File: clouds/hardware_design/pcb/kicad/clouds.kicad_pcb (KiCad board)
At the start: 2 copper layers, 88.9 x 106 mm, 156 parts, among them IC1 74HC595D, IC10 TL072D, IC2 LM1117-3.3, IC3 MCP6002, IC4 MCP6004, IC5 STM32F405RGT6, IC6 LM4040B10, IC7 LM1117-3.3, IC8 WM8731, IC9 TL072D, J1 PJ301_THONKICONN6, J10 PJ301_THONKICONN6, J11 PJ301_THONKICONN6, J12 PJ301_THONKICONN6, J2 PJ301_THONKICONN6, J3 PJ301_THONKICONN6, J4 PJ301_THONKICONN6, J5 PJ301_THONKICONN6, J6 PJ301_THONKICONN6, J7 PJ301_THONKICONN6, J8 PJ301_THONKICONN6, J9 PJ301_THONKICONN6, Q1 MMBT3904, Q2 MMBT3904, Q3 8MHz, Q4 12.288MHz, SW1 LP4OA1PBCT

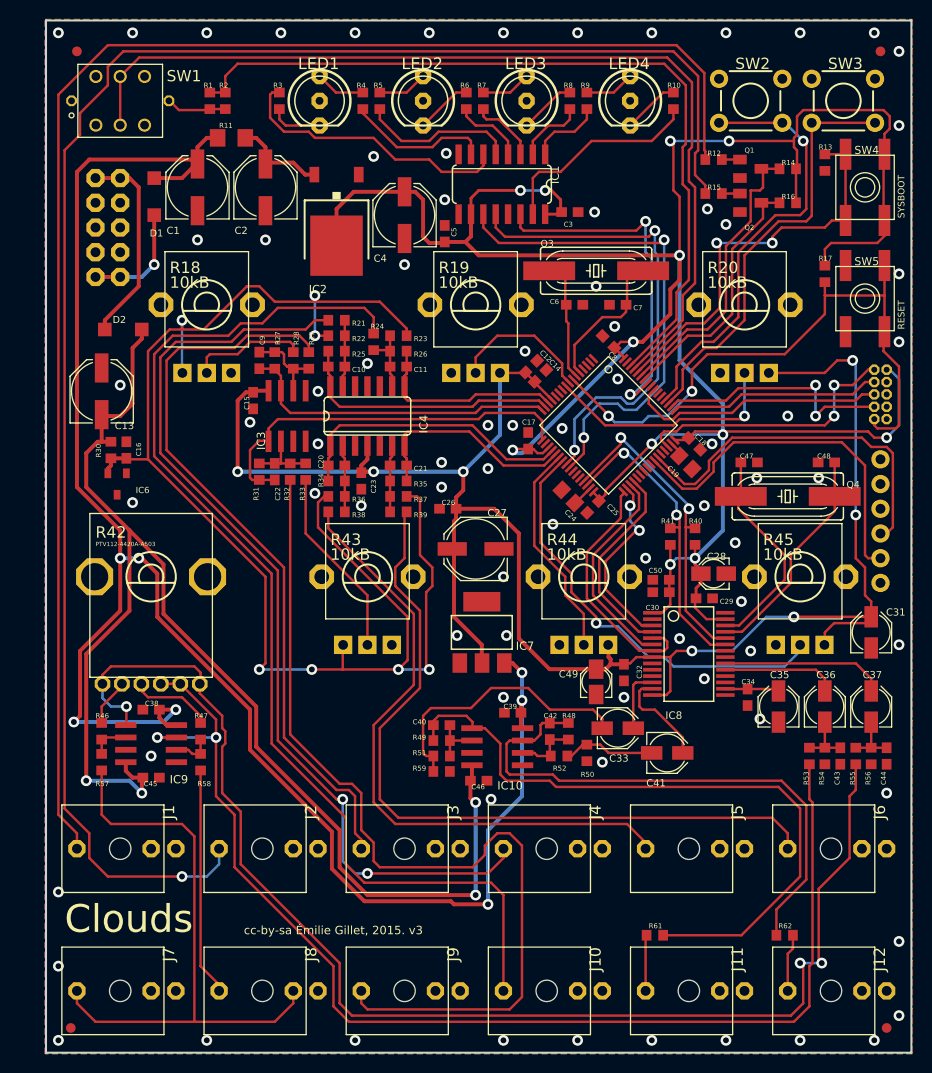
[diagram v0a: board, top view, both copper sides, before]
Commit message: clouds wm8731 QFN on PCB. also panasonic a -> b caps
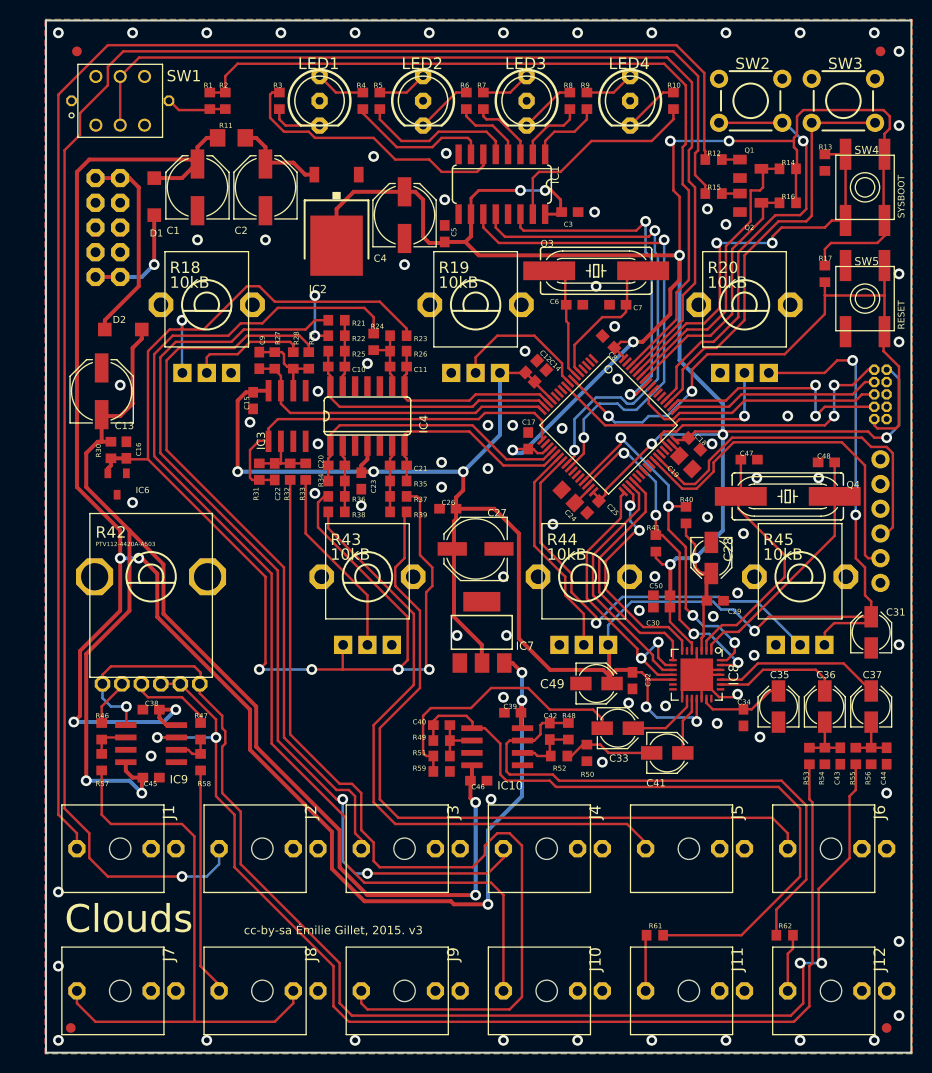
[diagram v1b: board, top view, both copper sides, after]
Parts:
- removed U$2: , clouds:ROHS_BIG
- C28, C49: footprint clouds:PANASONIC_A -> clouds:PANASONIC_B
- IC1: value 74HC595D -> 74595D
- IC8: footprint clouds:SSOP28 -> Package_DFN_QFN:QFN-28-1EP_5x5mm_P0.5mm_EP3.35x3.35mm
- JP1: value (none) -> M06SIP
- SW2, SW3: value (none) -> TAC_SWITCHPTH
- SW4, SW5: value (none) -> EVQQ2
- moved R40 2.39 mm to (169.8, 102.8)
- moved C34 2.13 mm to (175.7, 123.6)
- moved IC8 1.99 mm to (170.9, 119.2)
- moved R41 1.64 mm to (166.7, 105.7)
- moved C28 1.63 mm to (172.4, 107.2), turned to -90 degrees
- moved C30 1.58 mm to (167.3, 112.3)
- moved C50 1.58 mm to (167.3, 111.0)
- moved C32 1.20 mm to (164.3, 119.8)
- moved C29 1.15 mm to (172.8, 111.6)
- moved C47 0.28 mm to (176.3, 97.1)
- moved C49 0.18 mm to (160.6, 120.1), turned to 0 degrees
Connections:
- net BOOT_FLASH renamed /clouds_2/BOOT_FLASH
- net JTCK renamed /clouds_2/JTCK
- net JTDI renamed /clouds_2/JTDI
- net JTDO renamed /clouds_2/JTDO
- net JTMS renamed /clouds_2/JTMS
- net LOUT_JACK renamed Net-(J11-PadP3)
- net RESET renamed /clouds_2/RESET
- net ROUT_JACK renamed Net-(J12-PadP3)
- net RX renamed /clouds_2/RX
- net TX renamed /clouds_2/TX
- C34 pad 1: N$17 -> Net-(C34-Pad1)
- C35 pad +: N$17 -> Net-(C34-Pad1)
- C47 pad 2: N$59 -> Net-(C47-Pad2)
- C48 pad 2: N$60 -> Net-(C48-Pad2)
- IC1 pad 9: (no net) -> unconnected-(IC1-Pad9)
- IC5 pad 10: (no net) -> unconnected-(IC5-Pad10)
- IC5 pad 11: (no net) -> unconnected-(IC5-Pad11)
- IC5 pad 2: (no net) -> unconnected-(IC5-Pad2)
- IC5 pad 27: (no net) -> unconnected-(IC5-Pad27)
- IC5 pad 29: I2C_SCL -> /clouds_2/I2C_SCL
- IC5 pad 3: (no net) -> unconnected-(IC5-Pad3)
- IC5 pad 30: I2C_SDA -> /clouds_2/I2C_SDA
- IC5 pad 33: I2S_LRCK -> /clouds_2/I2S_LRCK
- IC5 pad 34: I2S_SCK -> /clouds_2/I2S_SCK
- IC5 pad 35: I2S_SIN -> /clouds_2/I2S_SIN
- IC5 pad 36: I2S_SOUT -> /clouds_2/I2S_SOUT
- IC5 pad 37: (no net) -> unconnected-(IC5-Pad37)
- IC5 pad 38: (no net) -> unconnected-(IC5-Pad38)
- IC5 pad 39: (no net) -> unconnected-(IC5-Pad39)
- IC5 pad 4: (no net) -> unconnected-(IC5-Pad4)
- IC5 pad 40: (no net) -> unconnected-(IC5-Pad40)
- IC5 pad 41: (no net) -> unconnected-(IC5-Pad41)
- IC5 pad 44: (no net) -> unconnected-(IC5-Pad44)
- IC5 pad 45: (no net) -> unconnected-(IC5-Pad45)
- IC5 pad 53: (no net) -> unconnected-(IC5-Pad53)
- IC5 pad 54: (no net) -> unconnected-(IC5-Pad54)
- IC5 pad 56: (no net) -> unconnected-(IC5-Pad56)
- IC8 pad 1: +3V3 -> Net-(C48-Pad2)
- IC8 pad 10: (no net) -> /clouds_2/I2S_SIN
- IC8 pad 11: GND -> /clouds_2/I2S_LRCK
- IC8 pad 12: LOUT -> +3V3_A
- IC8 pad 13: ROUT -> unconnected-(IC8-Pad13)
- IC8 pad 14: +3V3_A -> unconnected-(IC8-Pad14)
- IC8 pad 16: N$17 -> LOUT
- IC8 pad 17: (no net) -> ROUT
- IC8 pad 18: (no net) -> +3V3_A
- IC8 pad 19: RIN -> GND
- IC8 pad 2: (no net) -> Net-(C47-Pad2)
- IC8 pad 20: LIN -> Net-(C34-Pad1)
- IC8 pad 21: GND -> unconnected-(IC8-Pad21)
- IC8 pad 22: GND -> unconnected-(IC8-Pad22)
- IC8 pad 23: I2C_SDA -> RIN
- IC8 pad 24: I2C_SCL -> LIN
- IC8 pad 25: N$60 -> GND
- IC8 pad 26: N$59 -> GND
- IC8 pad 27: +3V3 -> /clouds_2/I2C_SDA
- IC8 pad 28: GND -> /clouds_2/I2C_SCL
- IC8 pad 3: I2S_SCK -> +3V3
- IC8 pad 4: I2S_SOUT -> GND
- IC8 pad 5: I2S_LRCK -> +3V3
- IC8 pad 6: I2S_SIN -> unconnected-(IC8-Pad6)
- IC8 pad 7: I2S_LRCK -> /clouds_2/I2S_SCK
- IC8 pad 8: +3V3_A -> /clouds_2/I2S_SOUT
- IC8 pad 9: (no net) -> /clouds_2/I2S_LRCK
- J10 pad P2: (no net) -> unconnected-(J10-PadP2)
- J11 pad P2: (no net) -> unconnected-(J11-PadP2)
- J12 pad P2: (no net) -> unconnected-(J12-PadP2)
- J3 pad P2: (no net) -> unconnected-(J3-PadP2)
- J4 pad P2: (no net) -> unconnected-(J4-PadP2)
- J5 pad P2: (no net) -> unconnected-(J5-PadP2)
- J6 pad P2: (no net) -> unconnected-(J6-PadP2)
- J7 pad P2: (no net) -> unconnected-(J7-PadP2)
- J9 pad P2: (no net) -> unconnected-(J9-PadP2)
- JP1 pad 2: (no net) -> unconnected-(JP1-Pad2)
- JP1 pad 3: (no net) -> unconnected-(JP1-Pad3)
- JP1 pad 6: (no net) -> unconnected-(JP1-Pad6)
- JP2 pad 7: (no net) -> unconnected-(JP2-Pad7)
- Q4 pad 1: N$59 -> Net-(C47-Pad2)
- Q4 pad 2: N$60 -> Net-(C48-Pad2)
- R40 pad 1: I2C_SCL -> /clouds_2/I2C_SCL
- R41 pad 1: I2C_SDA -> /clouds_2/I2C_SDA
- SW1 pad P1: (no net) -> unconnected-(SW1-PadP1)
- SW1 pad P4: (no net) -> unconnected-(SW1-PadP4)
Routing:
- net /clouds_2/I2C_SCL: track 0.00 -> 37.5 mm, vias 0 -> 4
- net /clouds_2/I2C_SDA: track 0.00 -> 35.0 mm, vias 0 -> 4
- net I2C_SCL: track 33.2 -> 0.00 mm, vias 2 -> 0
- net I2C_SDA: track 31.3 -> 0.00 mm, vias 2 -> 0
- net /clouds_2/I2S_LRCK: track 0.00 -> 30.8 mm, vias 0 -> 2
- net I2S_LRCK: track 25.5 -> 0.00 mm
- net /clouds_2/I2S_SOUT: track 0.00 -> 25.5 mm
- net /clouds_2/I2S_SIN: track 0.00 -> 25.4 mm
- net Net-(C48-Pad2): track 0.00 -> 25.2 mm
- net Net-(C47-Pad2): track 0.00 -> 25.0 mm
- net /clouds_2/I2S_SCK: track 0.00 -> 23.9 mm, vias 0 -> 2
- net N$60: track 23.2 -> 0.00 mm
- net N$59: track 22.3 -> 0.00 mm
- net I2S_SIN: track 21.9 -> 0.00 mm
- net I2S_SOUT: track 21.1 -> 0.00 mm
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
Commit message: cap spacing
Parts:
- moved C32 0.20 mm to (164.5, 119.8)
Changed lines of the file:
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@@
   )
   (footprint "clouds:C0603" (layer "F.Cu")
-    (at 164.3 119.8 -90)
+    (at 164.5 119.8 -90)
     (descr "<b>CAPACITOR</b>")
     (property "Sheetfile" "clouds_2.kicad_sch")
@@
   (segment (start 143.8411 129.1336) (end 143.8411 127.5461) (width 0.254) (layer "F.Cu") (net 14))
   (segment (start 152.6286 104.6861) (end 152.6286 115.4811) (width 0.4064) (layer "F.Cu") (net 15))
-  (segment (start 162.6 118.7) (end 164.05 118.7) (width 0.4064) (layer "F.Cu") (net 15))
   (segment (start 161.9 120.1) (end 161.9 119.4) (width 0.4064) (layer "F.Cu") (net 15))
   (segment (start 137.0711 97.0661) (end 137.0711 95.6945) (width 0.4064) (layer "F.Cu") (net 15))
@@
   (segment (start 186.9186 86.9061) (end 185.3311 86.9061) (width 0.254) (layer "F.Cu") (net 15))
   (segment (start 188.8236 111.6711) (end 188.1886 111.0361) (width 0.254) (layer "F.Cu") (net 15))
-  (segment (start 164.05 118.7) (end 164.3 118.95) (width 0.4064) (layer "F.Cu") (net 15))
   (segment (start 145.9611 103.4161) (end 145.9611 106.0961) (width 0.4064) (layer "F.Cu") (net 15))
   (segment (start 188.1886 108.1786) (end 187.2361 107.2261) (width 0.254) (layer "F.Cu") (net 15))
+  (segment (start 162.35 118.95) (end 164.3 118.95) (width 0.4064) (layer "F.Cu") (net 15))
   (segment (start 150.0886 102.1461) (end 152.6286 104.6861) (width 0.4064) (layer "F.Cu") (net 15))
   (segment (start 161.9 116.235) (end 161.7961 116.1311) (width 0.4064) (layer "F.Cu") (net 15))
@@
   (segment (start 145.9611 113.2586) (end 148.8186 116.1161) (width 0.4064) (layer "F.Cu") (net 15))
   (segment (start 187.2361 107.2261) (end 187.2361 102.7811) (width 0.254) (layer "F.Cu") (net 15))
+  (segment (start 161.9 119.4) (end 162.35 118.95) (width 0.4064) (layer "F.Cu") (net 15))
   (segment (start 185.3311 86.9061) (end 184.0461 88.1911) (width 0.254) (layer "F.Cu") (net 15))
   (segment (start 123.7361 98.3361) (end 123.7361 91.0336) (width 0.4064) (layer "F.Cu") (net 15))
@@
   (segment (start 188.1886 111.0361) (end 188.1886 108.1786) (width 0.254) (layer "F.Cu") (net 15))
   (segment (start 146.9136 98.3361) (end 146.9136 100.2411) (width 0.4064) (layer "F.Cu") (net 15))
-  (segment (start 161.9 119.4) (end 162.6 118.7) (width 0.4064) (layer "F.Cu") (net 15))
   (segment (start 136.4361 97.7011) (end 137.0711 97.0661) (width 0.4064) (layer "F.Cu") (net 15))
   (segment (start 123.7361 91.0336) (end 124.5861 90.1836) (width 0.4064) (layer "F.Cu") (net 15))

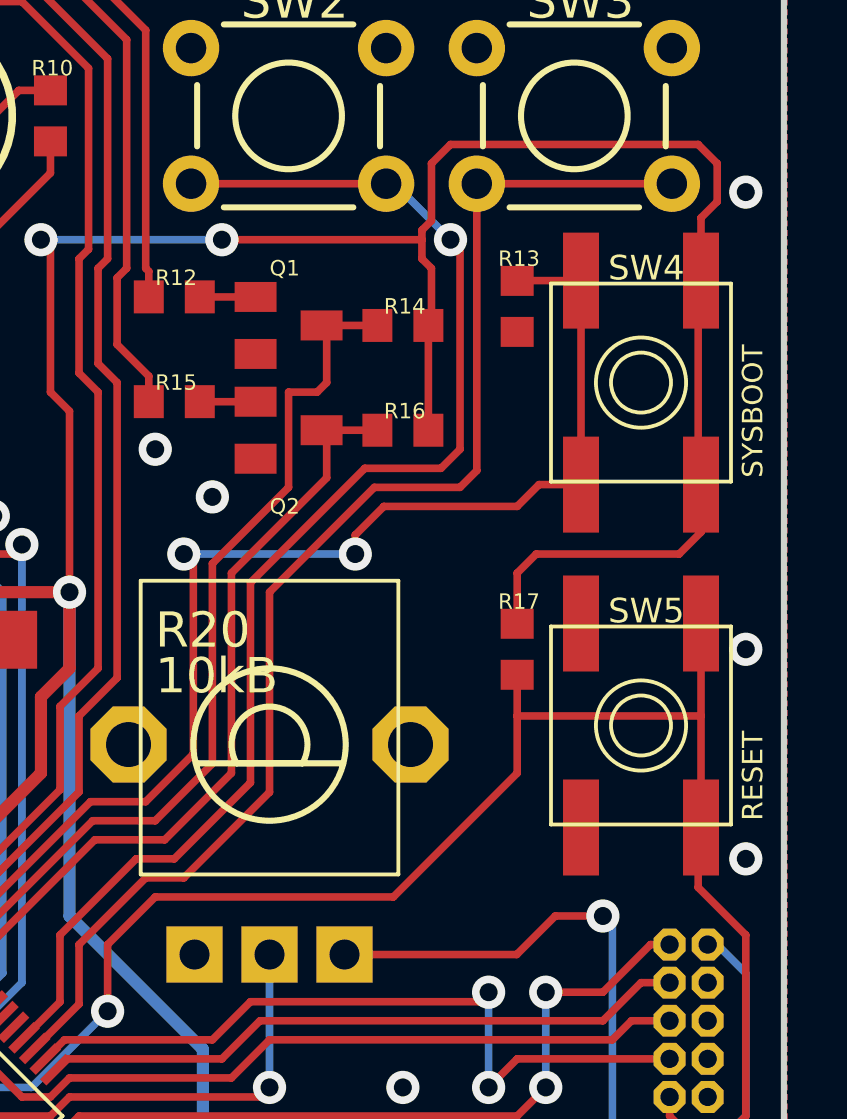
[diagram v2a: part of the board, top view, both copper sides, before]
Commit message: clouds SMD reset + boot buttons
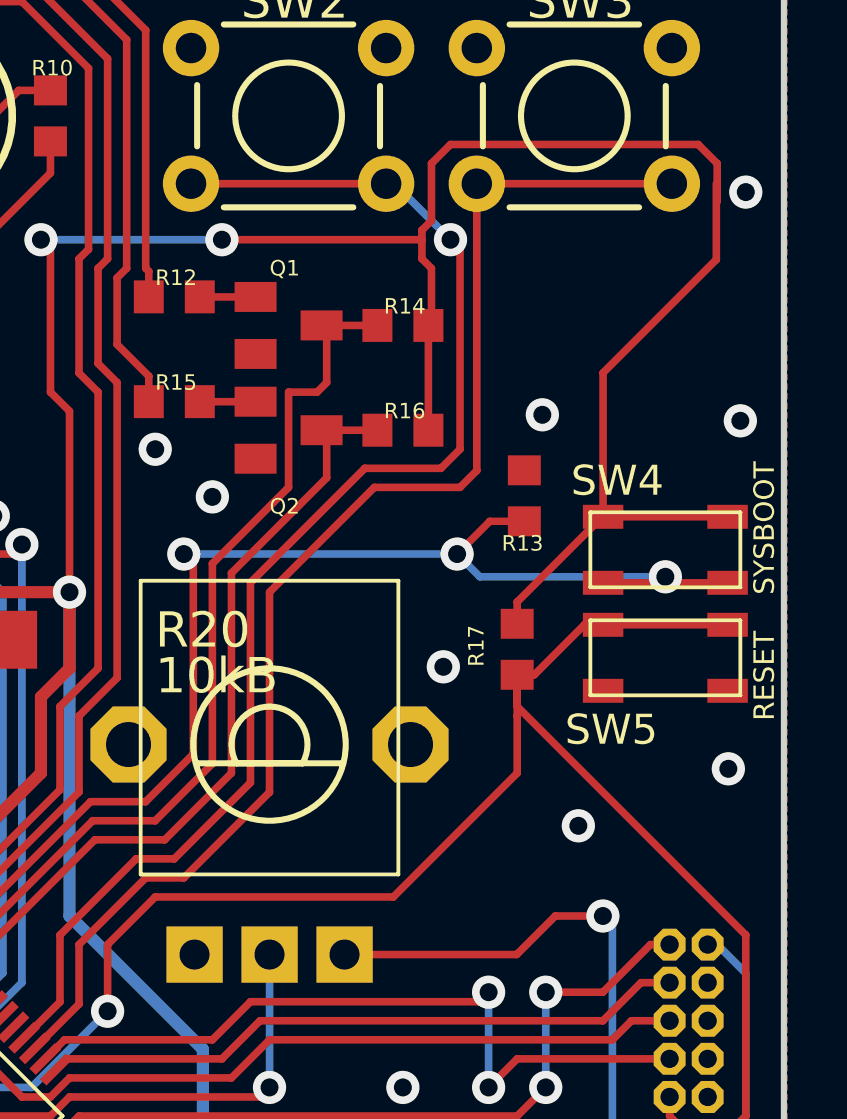
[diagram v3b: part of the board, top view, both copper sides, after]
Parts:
- SW4, SW5: footprint clouds:EVQ-Q2 -> Supercell 1.3:k2-1808 pushbutton switch
- moved R13 6.32 mm to (184.3, 72.9), turned to -90 degrees
- moved SW4 5.63 mm to (189.0, 74.7), turned to 0 degrees
- moved SW5 2.40 mm to (189.0, 78.3), turned to 0 degrees
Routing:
- net /clouds_2/RESET: track 63.5 -> 66.0 mm
- net +3V3: track 274.6 -> 276.4 mm
- net /clouds_2/BOOT_FLASH: track 41.5 -> 41.2 mm, vias 2 -> 3
- net GND: vias 82 -> 85

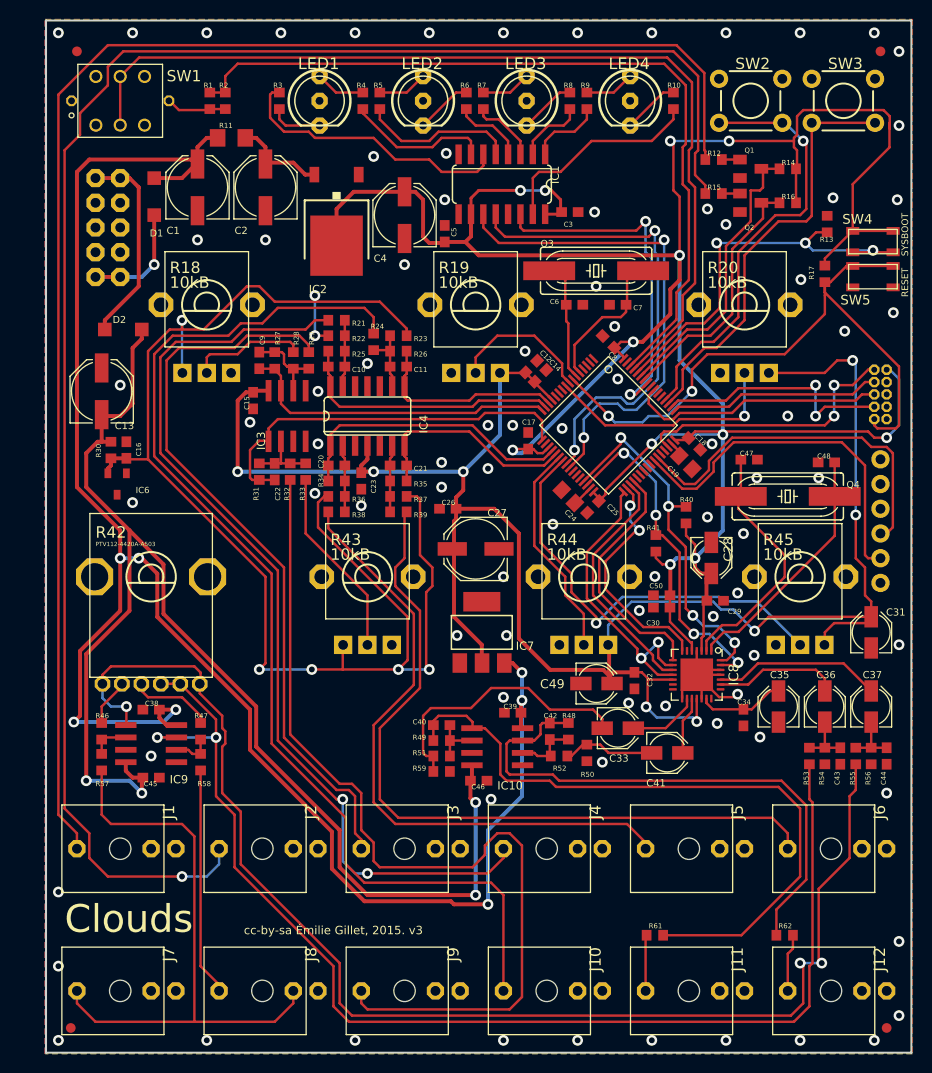
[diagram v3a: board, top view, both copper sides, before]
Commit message: clouds new kind of LED/switch pushbutton
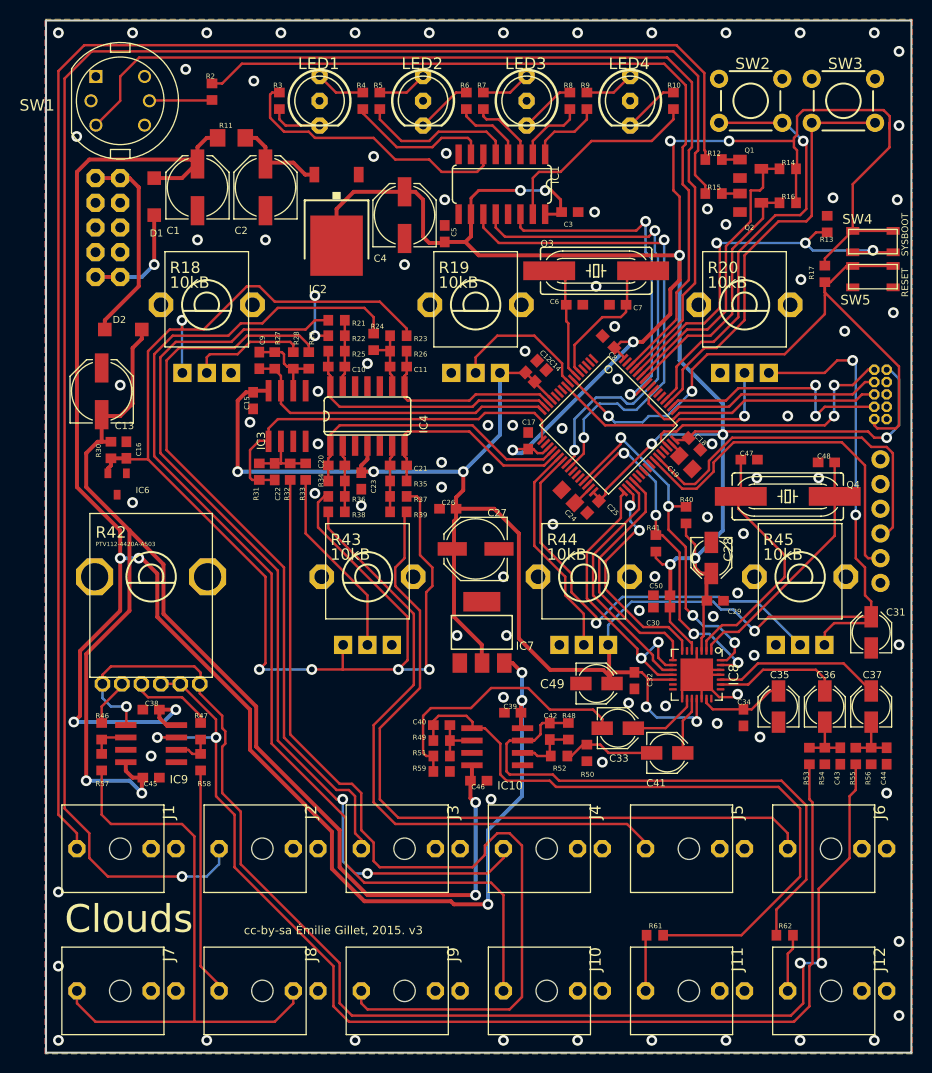
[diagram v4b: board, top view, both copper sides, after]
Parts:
- removed F1, F2, F3, F4: FIDUCIAL1X2, clouds:FIDUCIAL-1X2
- removed R1: 68, clouds:R0603
- R2: value 68 -> 1k
- SW1: value LP4OA1PBCT -> SW_Push_LED; footprint clouds:LP4OA1PBCT -> Supercell 1.3:C&K_D6R
- moved R2 1.66 mm to (121.1, 59.3)
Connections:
- R2 pad 2: Net-(R1-Pad2) -> Net-(R2-Pad2)
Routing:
- net Net-(R2-Pad2): track 0.00 -> 6.46 mm
- net Net-(R1-Pad2): track 6.01 -> 0.00 mm
- net Net-(J2-PadP3): track 175.4 -> 177.3 mm
- net LED_REC: track 83.7 -> 82.1 mm
- net Net-(J1-PadP3): track 156.8 -> 158.3 mm
- net SW_REC: track 98.0 -> 99.1 mm
- net GND: vias 85 -> 88
